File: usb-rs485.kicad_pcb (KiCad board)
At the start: 4 copper layers, 27.5 x 35.8 mm, 91 parts, among them IC1 THVD2450VDRCR, IC2 THVD2450VDRCR, IC3 THVD2450VDRCR, J1 USB4110GFA, M1 THRU_HOLE_PAD, M2 THRU_HOLE_PAD, Q1 SSM3K15F,LF, Q2 SSM3K15F,LF, U1 C2901617, U10 TPS63070, U11 TPS63070, U12 DF52-4S-0.8H(21), U13 DF52-4S-0.8H(21), U14 DF52-4S-0.8H(21), U2 STM32G431CBT6, U3 TLE9250XSJXUMA1, U4 DF52-3S-0.8H(21), U5 DF52-4S-0.8H(21), U6 SPX3819M5-L-5-0, U7 DF52-8S-0.8H(21), U8 ESP32-WROOM-32E-H4, U9 CP2102N-A02-GQFN24R

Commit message: backups removalled schematic looking correct if not good
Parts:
- removed C11, C13, C22, C24, C25, C27, C29, C30, C32, C33, C34: 10uF 0603, robot-cortex:C_0603_1608Metric
- removed C12, C14, C15, C23, C26, C35: 100nF, robot-cortex:C_0402_1005Metric
- removed C31, C36, C37, C38: 100nF, Capacitor_SMD:C_0402_1005Metric
- removed D6: NSR0530HT1G, robot-cortex:SOD2512X110N
- removed D7: 150060GS84000, robot-cortex:LED_0603_1608Metric
- removed D8: ESD9B3.3ST5G, robot-cortex:D_SOD-923
- removed IC2, IC3: THVD2450VDRCR, robot-cortex:THVD2410VDRCR
- removed L1, L2: 1uH, robot-cortex:L_1210_3225Metric
- removed M1, M2: THRU_HOLE_PAD, robot-cortex:TEARDROP
- removed Q1, Q2: SSM3K15F,LF, robot-cortex:SOT-23-3
- removed R10: 470k, robot-cortex:R_0402_1005Metric
- removed R11: 150k, robot-cortex:R_0402_1005Metric
- removed R12, R15: 100k, robot-cortex:C_0402_1005Metric
- removed R13: 680k, robot-cortex:R_0402_1005Metric
- removed R14: 130k, robot-cortex:R_0402_1005Metric
- removed R16: 0, robot-cortex:R_0402_1005Metric
- removed R17: 470, robot-cortex:R_0402_1005Metric
- removed R18: 4.7k, robot-cortex:R_0402_1005Metric
- removed R20, R21: 120, robot-cortex:R_0402_1005Metric
- removed R4, R5, R6: 10k, robot-cortex:R_0402_1005Metric
- removed U1: C2901617, robot-cortex:ECS-1633-480-BN-TR
- removed U10, U11: TPS63070, robot-cortex:VQFN-TPS63070
- removed U13, U14, U5: DF52-4S-0.8H(21), robot-cortex:DF52-4S-0.8H(21)
- removed U2: STM32G431CBT6, robot-cortex:LQFP48-STM32
- removed U3: TLE9250XSJXUMA1, robot-cortex:SOIC8-TLE5009
- removed U4: DF52-3S-0.8H(21), robot-cortex:DF52-3S-0.8H(21)
- removed U6: SPX3819M5-L-5-0, robot-cortex:SOT-23-5
- removed U7: DF52-8S-0.8H(21), robot-cortex:DF52-8S-0.8H(21)
- removed U8: ESP32-WROOM-32E-H4, robot-cortex:ESP32-WROOM-32
- C1, C10, C17, C18, C2, C20, C21, C28, C3, C4, C5, C6, C8, C9, D1, D2, D3, D5, IC1, J1, R1, R19, R7, R8, R9, U12, U9: moved to F.Cu
- C16, C19, C7, D4, R3: moved to B.Cu
- R2: value 4.7k -> 470; moved to F.Cu
- moved C18 86.4 mm to (130.3, 94.4)
- moved C19 84.9 mm to (131.5, 99.1), turned to 180 degrees
- moved C16 84.9 mm to (131.4, 97.4), turned to 180 degrees
- moved C3 84.5 mm to (131.3, 109.4)
- moved C17 84.0 mm to (131.5, 94.4)
- moved R2 82.1 mm to (132.1, 109.4), turned to -90 degrees
- moved C2 80.5 mm to (133.1, 109.5), turned to -90 degrees
- moved C6 79.4 mm to (134.2, 109.5), turned to -90 degrees
- moved R3 79.0 mm to (134.0, 115.6), turned to 180 degrees
- moved C8 77.1 mm to (135.0, 109.4), turned to -90 degrees
- moved D4 74.8 mm to (136.1, 115.1), turned to 0 degrees
- moved C20 70.0 mm to (138.5, 100.7), turned to 180 degrees
- moved C21 69.5 mm to (138.7, 101.6), turned to 180 degrees
- moved C10 69.1 mm to (139.0, 116.1), turned to 180 degrees
- moved R8 69.0 mm to (139.0, 99.4), turned to 0 degrees
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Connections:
- net /D+ renamed /CP2102N/D+
- net /D- renamed /CP2102N/D-
- net /ESP32/CP210x_VBUS renamed /CP2102N/CP210x_VBUS
- C20 pad 1: +3V3 -> /VUSB
- C21 pad 1: +3V3 -> /VUSB
- C28 pad 2: /+5V0 -> /VUSB
- D4 pad 1: Net-(D4-K) -> /RX
- D4 pad 2: /LED -> Net-(D4-A)
- IC1 pad 10: /+5V0 -> /VUSB
- IC1 pad 2: /UART1_RX -> /RX
- IC1 pad 3: /UART1_DE -> /DE
- IC1 pad 4: /UART1_DE -> /DE
- IC1 pad 5: /UART1_TX -> /TX
- R2 pad 1: /NRST -> +3V3
- R2 pad 2: GND -> Net-(D4-A)
- R3 pad 1: Net-(D4-K) -> +3V3
- R3 pad 2: GND -> Net-(D5-A)
- U12 pad 1: /VBAT -> /VUSB
- U9 pad 12: unconnected-(U9-GPIO.2/RS485-Pad12) -> /DE
- U9 pad 19: /ESP32/RTS -> unconnected-(U9-~{RTS}-Pad19)
- U9 pad 20: /ESP32/CP210x_RX -> /RX
- U9 pad 21: /ESP32/CP210x_TX -> /TX
- U9 pad 23: /ESP32/DTR -> /CP2102N/DTR
- U9 pad 7: +3V3 -> /VUSB
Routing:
- net /+5V0: track 76.9 -> 0.00 mm, vias 7 -> 0
- net /VBAT: track 60.7 -> 0.00 mm, vias 1 -> 0
- net +3V3: track 55.5 -> 7.66 mm, vias 21 -> 4
- net /ESP32/IO0: track 40.1 -> 0.00 mm, vias 5 -> 0
- net /ESP32/EN: track 30.5 -> 0.00 mm, vias 2 -> 0
- net /VDD_MIXED: track 29.8 -> 1.43 mm, vias 5 -> 2
- net /UART2_TX: track 23.0 -> 0.00 mm, vias 1 -> 0
- net /SWCLK: track 22.8 -> 0.00 mm, vias 2 -> 0
- net /SWDIO: track 21.6 -> 0.00 mm, vias 2 -> 0
- net /ESP32/CP210x_RX: track 20.7 -> 0.00 mm, vias 1 -> 0
- net /ESP32/DTR: track 19.9 -> 0.00 mm, vias 2 -> 0
- net /UART2_RX: track 19.0 -> 0.00 mm, vias 1 -> 0
- net /ESP32/RTS: track 18.4 -> 0.00 mm, vias 2 -> 0
- net /UART1_RX: track 17.8 -> 0.00 mm, vias 2 -> 0
- net /ESP32/CP210x_TX: track 17.3 -> 0.00 mm, vias 1 -> 0
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- removed copper zone on B.Cu, net +3V3
- removed copper zone on In2.Cu, net +3V3
- removed copper zone on F.Cu, net /+5V0
- removed copper zone on F.Cu, net /VDD_MIXED
- removed copper zone on F.Cu, net Net-(U10-L1)
- removed copper zone on F.Cu, net Net-(U10-L2)
- removed copper zone on F.Cu, net Net-(U11-L1)
- removed copper zone on F.Cu, net Net-(U11-L2)
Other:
- outline, holes or cut-outs redrawn
- board text added: "5V0 A B GND"
- board text added: "V1R1"
- board text removed: "3V3"
- board text removed: "CH"
- board text removed: "CL"
- board text removed: "EN"
- board text removed: "GND"
- board text removed: "IO0"
- board text removed: "SWCLK"
- board text removed: "SWDIO"
- board text removed: "TCK"
- board text removed: "TDI"
- board text removed: "TDO"
- board text removed: "TMS"
- board text removed: "V3 R1"
- board text removed: "VBAT"
- board text removed: "Vbat A B GND"

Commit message: library table
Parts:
- C16, C19, C7, D4, R3: moved to F.Cu
- D5: value NSR0530HT1G -> 150060GS84000; footprint robot-cortex:SOD2512X110N -> robot-cortex:LED_0603_1608Metric
- moved D4 12.1 mm to (148.1, 113.1), turned to 180 degrees
- moved C7 3.35 mm to (144.2, 113.8), turned to 0 degrees
- moved D5 2.48 mm to (152.1, 113.2)
- turned C16 to 0 degrees
- turned C19 to 0 degrees
- turned R3 to 0 degrees
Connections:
- D5 pad 1: /VDD_MIXED -> /TX
- D5 pad 2: /VBAT -> Net-(D5-A)
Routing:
- net /VDD_MIXED: track 1.43 -> 0.00 mm, vias 2 -> 0
- net /TX: track 6.09 -> 7.52 mm, vias 1 -> 3

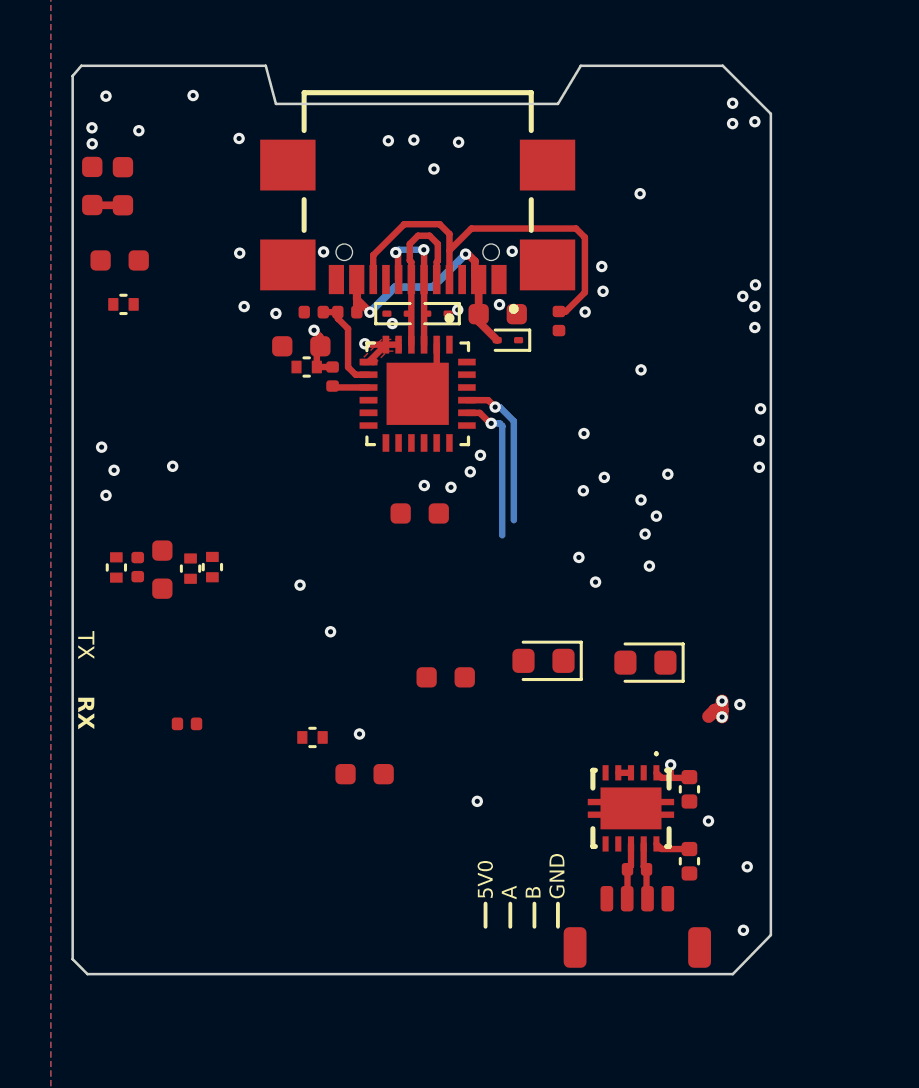
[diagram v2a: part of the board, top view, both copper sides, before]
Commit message: cleanup some routing
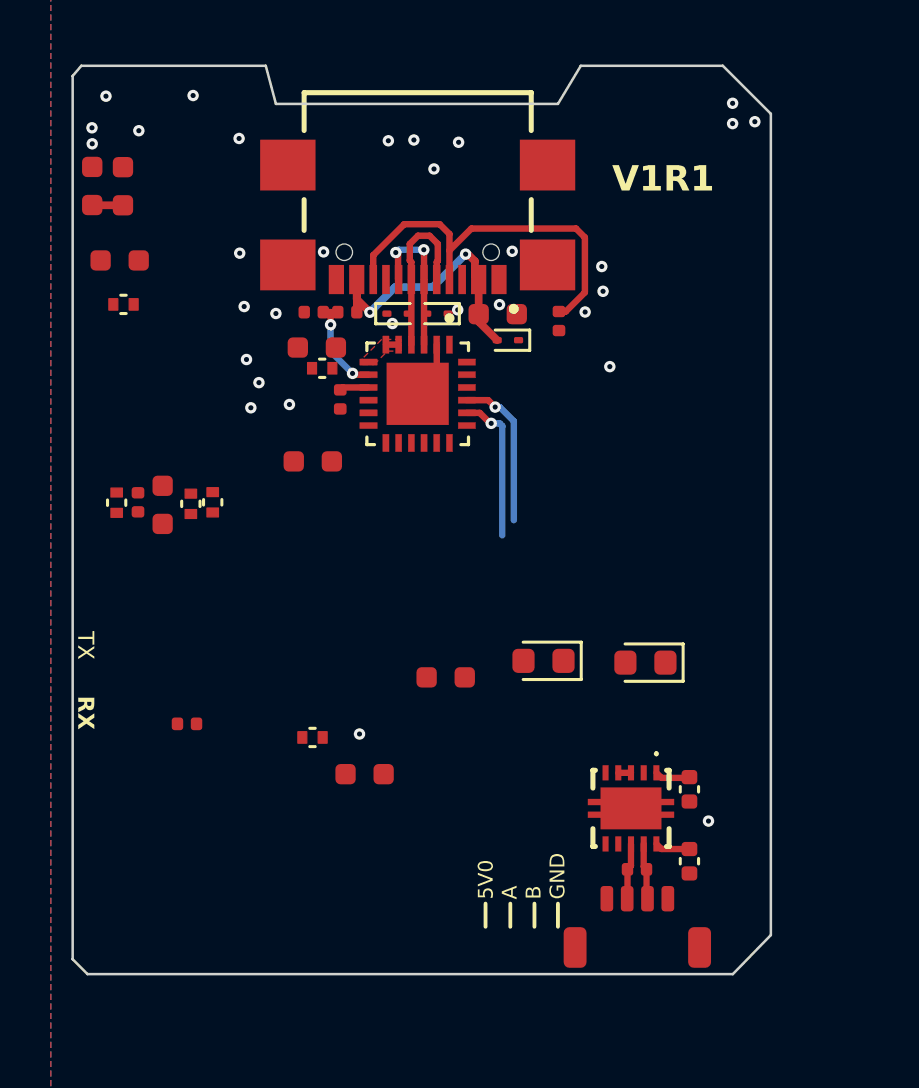
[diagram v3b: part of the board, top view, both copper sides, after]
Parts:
- moved C5 4.68 mm to (139.0, 105.3)
- moved C8 2.55 mm to (135.1, 106.9)
- moved R2 2.55 mm to (132.1, 106.9)
- moved C2 2.55 mm to (133.1, 107.0)
- moved C3 2.55 mm to (131.3, 106.9)
- moved C6 2.55 mm to (134.2, 106.9)
- moved R9 0.95 mm to (140.1, 102.8), turned to -90 degrees
- moved C20 0.61 mm to (139.2, 100.8)
- moved C21 0.61 mm to (139.4, 101.6)
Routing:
- net +3V3: track 7.66 -> 3.11 mm, vias 4 -> 0
- net /TX: track 7.52 -> 6.09 mm, vias 3 -> 1
- net /CP2102N/CP210x_VBUS: track 3.83 -> 4.27 mm, vias 0 -> 2
- net GND: vias 58 -> 31

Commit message: routing
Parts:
- removed C10, C19, C3, C6: 100nF, robot-cortex:C_0402_1005Metric
- removed C16, C17, C18: 4.7uF, robot-cortex:C_0603_1608Metric
- removed C2, C7: 10uF 0603, robot-cortex:C_0603_1608Metric
- C5: value 10uF 0603 -> 4.7uF 0603
- moved R2 14.3 mm to (146.4, 106.9), turned to 180 degrees
- moved D5 12.9 mm to (140.8, 106.9)
- moved C1 12.9 mm to (145.2, 108.6)
- moved IC1 12.9 mm to (142.9, 109.4)
- moved C28 12.9 mm to (145.2, 111.5)
- moved U12 12.9 mm to (143.1, 112.9)
- moved R19 12.9 mm to (143.1, 111.8)
- moved C9 10.2 mm to (146.3, 108.9), turned to -90 degrees
- moved R3 9.49 mm to (140.1, 108.3), turned to 90 degrees
- moved C8 8.06 mm to (139.6, 100.2), turned to 180 degrees
- moved D4 7.21 mm to (144.4, 106.9), turned to 0 degrees
- moved C5 4.24 mm to (139.6, 101.1), turned to 180 degrees
- moved C21 1.81 mm to (138.6, 103.2)
- moved R8 1.51 mm to (137.5, 99.4)
- moved C20 1.42 mm to (138.8, 102.2)
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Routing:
- net /VUSB: track 12.8 -> 40.0 mm, vias 2 -> 5
- net +3V3: track 3.11 -> 23.3 mm, vias 0 -> 4
- net /DE: track 0.50 -> 4.87 mm, vias 0 -> 2
- net /TX: track 6.09 -> 7.97 mm, vias 1 -> 2
- net /CP2102N/CP210x_VBUS: track 4.27 -> 6.11 mm
- net Net-(D5-A): track 0.00 -> 0.99 mm
- net Net-(D4-A): track 0.00 -> 0.81 mm
- net /CP2102N/D+: track 6.01 -> 6.67 mm
- net /CP2102N/D-: track 6.78 -> 7.35 mm
- net /RX: track 5.91 -> 5.98 mm, vias 1 -> 0
- net GND: vias 31 -> 38
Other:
- board size 27.5 x 35.8 mm -> 14.4 x 24.7 mm

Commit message: routed, thru holes. ready to order i think
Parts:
- added J2: ~, robot-cortex:ThruHoleBreadboardX4, F.Cu at (136.9, 108.0)
- added J3: ~, robot-cortex:ThruHoleBreadboardX4, F.Cu at (149.4, 108.0)
- moved R2 0.49 mm to (146.2, 107.3), turned to 90 degrees
- moved C9 0.39 mm to (146.2, 109.2)
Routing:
- net /RS485 Transceiver/RS1_B: track 2.22 -> 14.4 mm, vias 0 -> 2
- net /RX: track 5.98 -> 13.5 mm
- net /RS485 Transceiver/RS1_A: track 2.22 -> 8.99 mm
- net /VUSB: track 40.0 -> 44.8 mm
- net /TX: track 7.97 -> 12.7 mm
- net +3V3: track 23.3 -> 27.9 mm
- net GND: vias 38 -> 42
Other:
- board text added: "3V3"
- board text added: "5V"
- board text added: "A"
- board text added: "B"
- board text added: "GND"

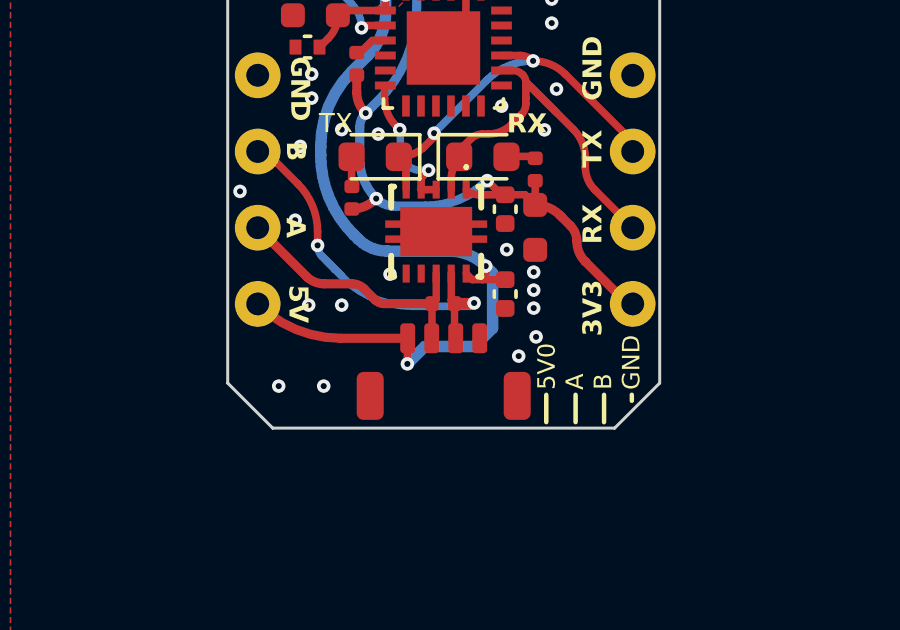
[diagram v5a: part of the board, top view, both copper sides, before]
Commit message: removed inner 2 and made it wavyy
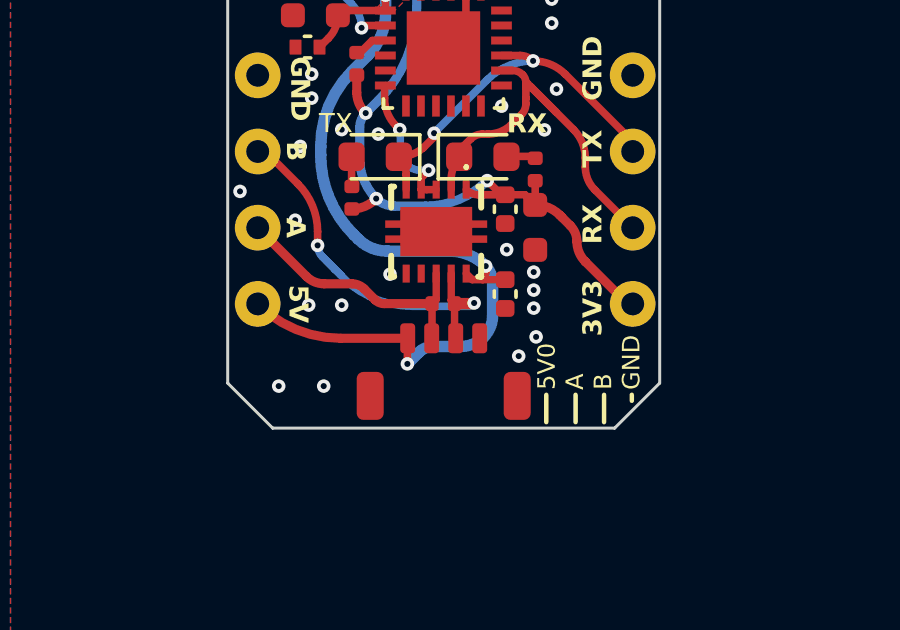
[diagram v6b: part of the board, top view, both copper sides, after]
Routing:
- removed copper zone on In1.Cu, net GND
- removed copper zone on In2.Cu, net GND
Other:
- copper layers 4 -> 2
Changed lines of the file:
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@@
   (layers
     (0 "F.Cu" signal)
-    (1 "In1.Cu" signal)
-    (2 "In2.Cu" signal)
     (31 "B.Cu" signal)
     (32 "B.Adhes" user "B.Adhesive")
@@
       (layer "F.Mask" (type "Top Solder Mask") (thickness 0.01))
       (layer "F.Cu" (type "copper") (thickness 0.035))
-      (layer "dielectric 1" (type "prepreg") (thickness 0.1) (material "FR4") (epsilon_r 4.5) (loss_tangent 0.02))
-      (layer "In1.Cu" (type "copper") (thickness 0.035))
-      (layer "dielectric 2" (type "core") (thickness 1.24) (material "FR4") (epsilon_r 4.5) (loss_tangent 0.02))
-      (layer "In2.Cu" (type "copper") (thickness 0.035))
-      (layer "dielectric 3" (type "prepreg") (thickness 0.1) (material "FR4") (epsilon_r 4.5) (loss_tangent 0.02))
+      (layer "dielectric 1" (type "core") (thickness 1.51) (material "FR4") (epsilon_r 4.5) (loss_tangent 0.02))
       (layer "B.Cu" (type "copper") (thickness 0.035))
       (layer "B.Mask" (type "Bottom Solder Mask") (thickness 0.01))
@@
   (arc (start 141.174098 101.662165) (mid 141.175285 101.668369) (end 141.175 101.674222) (width 0.254) (layer "F.Cu") (net 16))
   (arc (start 145.25956 97.28044) (mid 145.451019 97.566977) (end 145.51825 97.904972) (width 0.3048) (layer "F.Cu") (net 16))
-  (segment (start 144.74825 110.77) (end 144.51825 110.54) (width 0.381) (layer "B.Cu") (net 16))
   (segment (start 141.07825 99.786274) (end 141.07825 101.254539) (width 0.381) (layer "B.Cu") (net 16))
-  (segment (start 144.74825 112.61) (end 144.74825 110.77) (width 0.381) (layer "B.Cu") (net 16))
-  (segment (start 144.13825 113.22) (end 144.74825 112.61) (width 0.381) (layer "B.Cu") (net 16))
   (segment (start 141.184233 101.510404) (end 141.184233 102.09) (width 0.381) (layer "B.Cu") (net 16))
   (segment (start 140.594494 103.513756) (end 140.058895 104.049355) (width 0.381) (layer "B.Cu") (net 16))
-  (segment (start 142.48825 113.22) (end 144.13825 113.22) (width 0.381) (layer "B.Cu") (net 16))
-  (segment (start 141.90825 113.8) (end 142.48825 113.22) (width 0.381) (layer "B.Cu") (net 16))
+  (segment (start 144.74825 112.199879) (end 144.74825 111.095269) (width 0.381) (layer "B.Cu") (net 16))
+  (segment (start 141.90825 113.8) (end 142.29825 113.41) (width 0.381) (layer "B.Cu") (net 16))
   (segment (start 142.998763 98.41) (end 142.94119 98.41) (width 0.3048) (layer "B.Cu") (net 16))
+  (segment (start 142.75695 113.22) (end 143.685702 113.22) (width 0.381) (layer "B.Cu") (net 16))
   (segment (start 141.23825 99.4) (end 141.724125 98.914125) (width 0.3048) (layer "B.Cu") (net 16))
   (segment (start 144.20879 97.90879) (end 145.00458 97.113) (width 0.3048) (layer "B.Cu") (net 16))
@@
   (segment (start 140.114266 109.486015) (end 140.26825 109.64) (width 0.381) (layer "B.Cu") (net 16))
   (arc (start 144.20879 97.90879) (mid 143.653626 98.279739) (end 142.998763 98.41) (width 0.3048) (layer "B.Cu") (net 16))
+  (arc (start 142.29825 113.41) (mid 142.508703 113.26938) (end 142.75695 113.22) (width 0.381) (layer "B.Cu") (net 16))
   (arc (start 141.23825 99.4) (mid 141.119833 99.577224) (end 141.07825 99.786274) (width 0.381) (layer "B.Cu") (net 16))
   (arc (start 141.724125 98.914125) (mid 142.282519 98.541018) (end 142.94119 98.41) (width 0.3048) (layer "B.Cu") (net 16))
+  (arc (start 144.74825 111.095269) (mid 144.688475 110.79476) (end 144.51825 110.54) (width 0.381) (layer "B.Cu") (net 16))
   (arc (start 140.058895 104.049355) (mid 139.288706 105.202025) (end 139.01825 106.561691) (width 0.381) (layer "B.Cu") (net 16))
+  (arc (start 143.685702 113.22) (mid 144.103801 113.136835) (end 144.45825 112.9) (width 0.381) (layer "B.Cu") (net 16))
   (arc (start 143.311144 110.04) (mid 143.964425 110.169946) (end 144.51825 110.54) (width 0.381) (layer "B.Cu") (net 16))
+  (arc (start 144.45825 112.9) (mid 144.672881 112.578782) (end 144.74825 112.199879) (width 0.381) (layer "B.Cu") (net 16))
   (arc (start 139.01825 106.84) (mid 139.303095 108.272013) (end 140.114266 109.486015) (width 0.381) (layer "B.Cu") (net 16))
   (arc (start 141.184233 102.09) (mid 141.030965 102.860531) (end 140.594494 103.513756) (width 0.381) (layer "B.Cu") (net 16))
@@
     )
   )
-  (zone (net 2) (net_name "GND") (layers "F.Cu" "In1.Cu" "In2.Cu" "B.Cu") (hatch edge 0.5)
+  (zone (net 2) (net_name "GND") (layers "F&B.Cu") (hatch edge 0.5)
     (connect_pads (clearance 0.2))
     (min_thickness 0.2) (filled_areas_thickness no)
